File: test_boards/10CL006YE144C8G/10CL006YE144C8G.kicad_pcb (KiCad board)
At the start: 2 copper layers, 90 parts, among them IC1 10CL006YE144C8G, J1 CL_JTAG, U1 W25Q128JVS, Y1 SG-7050CAN

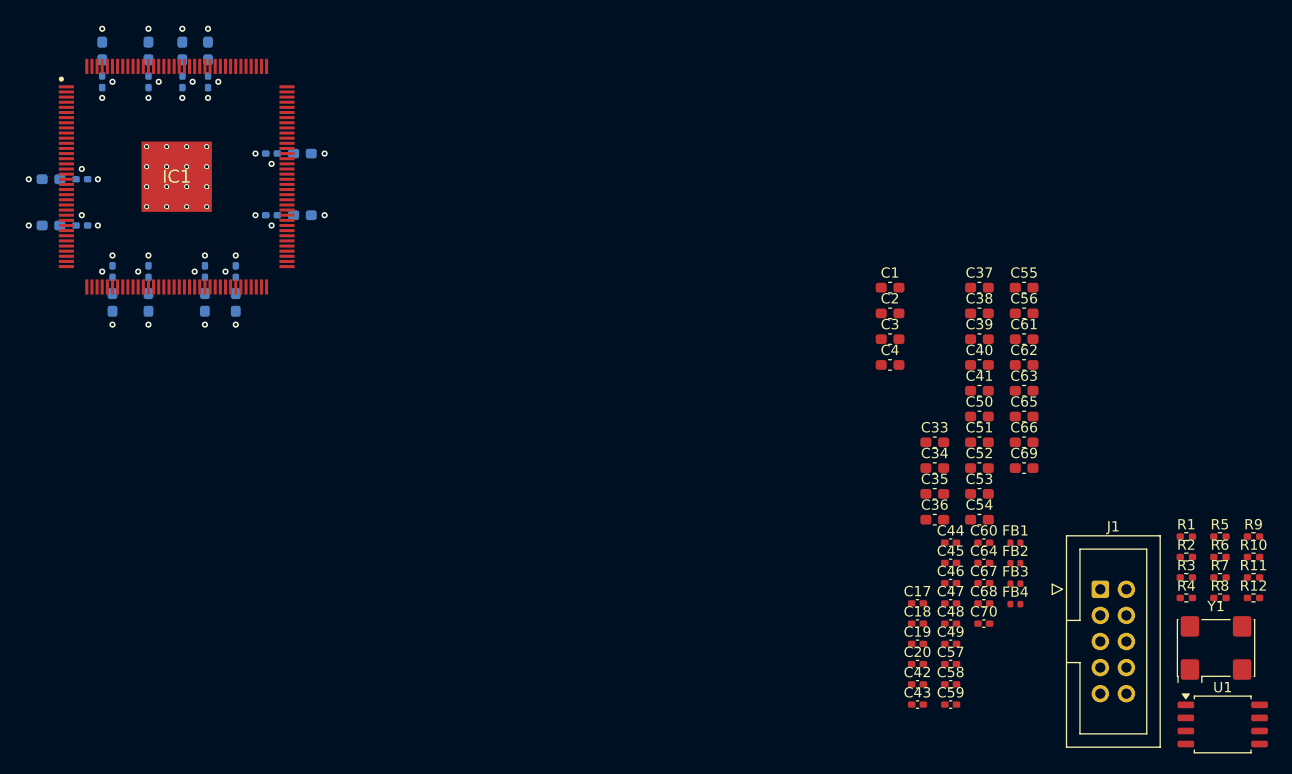
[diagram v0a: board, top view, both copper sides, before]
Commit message: Полный рефакторинг. components может быть несколько. Используются поля KiCad для компонент
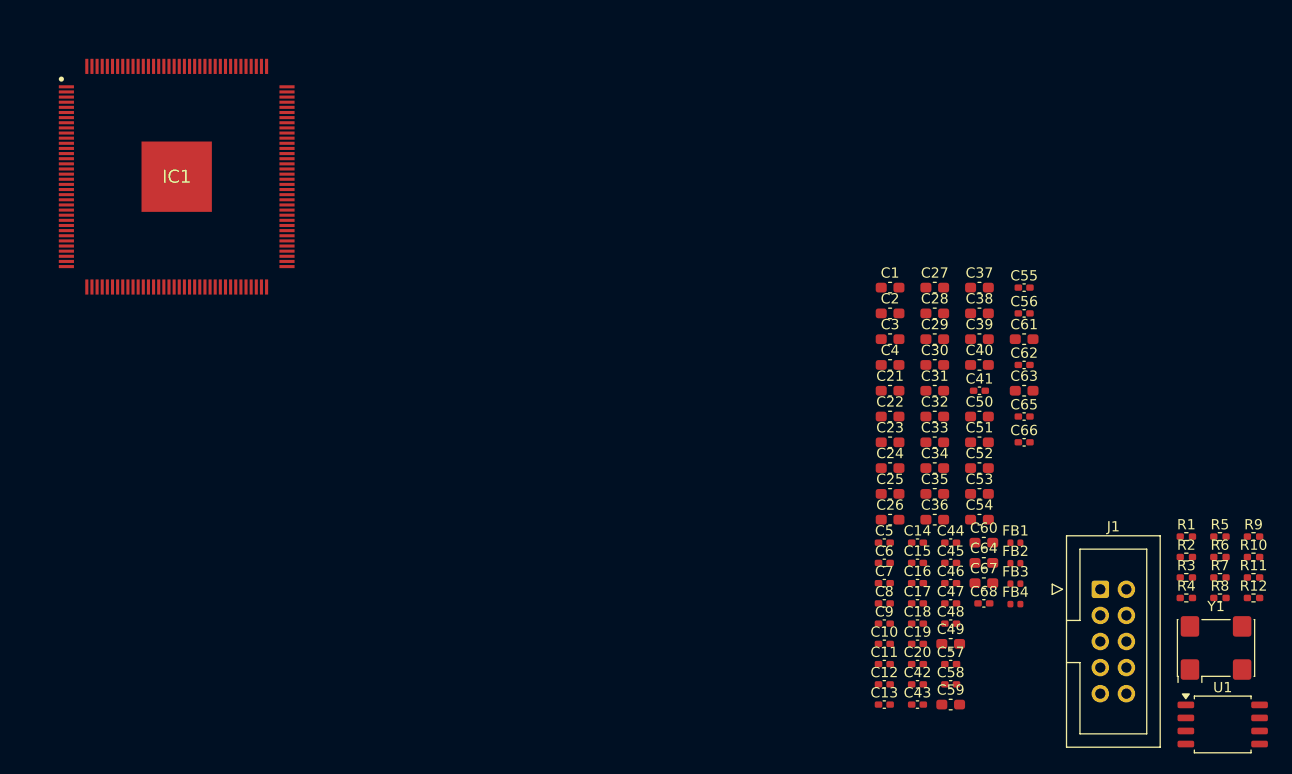
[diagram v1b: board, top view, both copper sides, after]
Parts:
- removed C69: 1uF, Capacitor_SMD:C_0603_1608Metric_Pad1.08x0.95mm_HandSolder
- removed C70: 100 nF, Capacitor_SMD:C_0402_1005Metric_Pad0.74x0.62mm_HandSolder
- C10, C11, C12, C13, C14, C15, C16, C21, C22, C23, C24, C25, C26, C27, C28, C29, C30, C31, C32, C5, C6, C7, C8, C9: moved to F.Cu
- C41, C55, C56, C62: value 4.7 uF -> 100 nF; footprint Capacitor_SMD:C_0603_1608Metric_Pad1.08x0.95mm_HandSolder -> Capacitor_SMD:C_0402_1005Metric_Pad0.74x0.62mm_HandSolder
- C49, C64, C67: value 100 nF -> 1uF; footprint Capacitor_SMD:C_0402_1005Metric_Pad0.74x0.62mm_HandSolder -> Capacitor_SMD:C_0603_1608Metric_Pad1.08x0.95mm_HandSolder
- C50: value 100 nF -> 1uF
- C53, C54: value 1uF -> 4.7 uF
- C59, C60: value 100 nF -> 4.7 uF; footprint Capacitor_SMD:C_0402_1005Metric_Pad0.74x0.62mm_HandSolder -> Capacitor_SMD:C_0603_1608Metric_Pad1.08x0.95mm_HandSolder
- C61: value 4.7 uF -> 1uF
- C65, C66: value 1uF -> 100 nF; footprint Capacitor_SMD:C_0603_1608Metric_Pad1.08x0.95mm_HandSolder -> Capacitor_SMD:C_0402_1005Metric_Pad0.74x0.62mm_HandSolder
- moved C16 93.2 mm to (149.7, 121.2), turned to 0 degrees
- moved C13 89.5 mm to (146.4, 133.0), turned to 0 degrees
- moved C32 88.5 mm to (151.4, 105.0), turned to 0 degrees
- moved C15 88.3 mm to (149.7, 119.2), turned to 0 degrees
- moved C5 85.8 mm to (146.4, 117.2)
- moved C6 84.7 mm to (146.4, 119.2)
- moved C14 84.5 mm to (149.7, 117.2), turned to 0 degrees
- moved C21 84.2 mm to (147.0, 102.4), turned to 0 degrees
- moved C22 83.8 mm to (147.0, 105.0), turned to 0 degrees
- moved C31 83.4 mm to (151.4, 102.4), turned to 0 degrees
- moved C7 81.0 mm to (146.4, 121.2), turned to 0 degrees
- moved C30 79.4 mm to (151.4, 99.9), turned to 0 degrees
- moved C12 78.9 mm to (146.4, 131.0), turned to 0 degrees
- moved C8 78.6 mm to (146.4, 123.1), turned to 0 degrees
- moved C23 76.9 mm to (147.0, 107.5), turned to 0 degrees
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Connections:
- C50 pad 1: +1V2_VCCINT -> +1V2_VCCD_PLL
- C51 pad 1: +1V2_VCCINT -> +2V5_VCCA
- C52 pad 1: +1V2_VCCD_PLL -> +3V3_VCCIO
- C53 pad 1: +2V5_VCCA -> +1V2_VCCD_PLL
- C54 pad 1: +3V3_VCCIO -> +1V2_VCCD_PLL
- C57 pad 1: +1V2_VCCD_PLL -> +2V5_VCCA
- C58 pad 1: +1V2_VCCD_PLL -> +2V5_VCCA
- C61 pad 1: +2V5_VCCA -> +3V3
- C62 pad 1: +2V5_VCCA -> +3V3
- C64 pad 1: +3V3 -> +3V3_OSCILL
- C66 pad 1: +3V3_OSCILL -> GND
- C66 pad 2: GND -> +3V3_OSCILL
- C67 pad 1: +3V3 -> +3V3_FLASH
- C68 pad 2: +3V3_OSCILL -> +3V3_FLASH
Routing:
- net GND: vias 40 -> 0
- net +3V3_VCCIO: vias 12 -> 0

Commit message: Проект переименован в KiCadSpoke
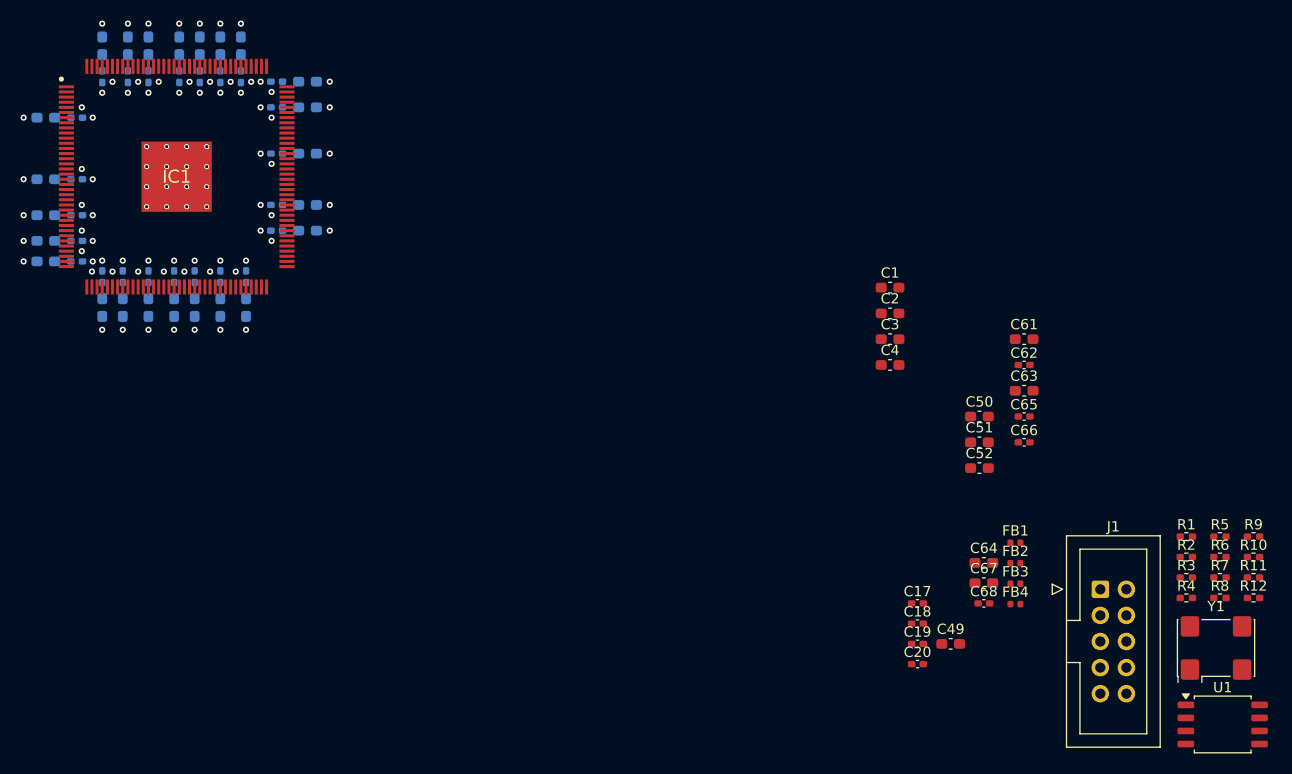
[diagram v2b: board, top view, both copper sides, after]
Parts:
- C10, C11, C12, C13, C14, C15, C16, C21, C22, C23, C24, C25, C26, C27, C28, C29, C30, C31, C32, C5, C57, C58, C59, C6, C60, C7, C8, C9: moved to B.Cu
- C33, C34, C35, C36, C37, C38, C39, C40, C53, C54: value 4.7 uF -> 100 nF; footprint Capacitor_SMD:C_0603_1608Metric_Pad1.08x0.95mm_HandSolder -> Capacitor_SMD:C_0402_1005Metric_Pad0.74x0.62mm_HandSolder; moved to B.Cu
- C41, C42, C43, C44, C45, C46, C47, C48, C55, C56: value 100 nF -> 4.7 uF; footprint Capacitor_SMD:C_0402_1005Metric_Pad0.74x0.62mm_HandSolder -> Capacitor_SMD:C_0603_1608Metric_Pad1.08x0.95mm_HandSolder; moved to B.Cu
- moved C59 98.1 mm to (64.8, 89.9), turned to 180 degrees
- moved C48 97.9 mm to (72.8, 68.9), turned to 90 degrees
- moved C42 95.2 mm to (64.8, 87.9), turned to 180 degrees
- moved C41 94.7 mm to (64.8, 75.9), turned to 180 degrees
- moved C57 93.7 mm to (67.8, 89.9)
- moved C16 93.4 mm to (70.3, 71.9), turned to -90 degrees
- moved C13 90.4 mm to (79.8, 71.9), turned to -90 degrees
- moved C55 89.8 mm to (70.3, 94.3), turned to -90 degrees
- moved C47 89.4 mm to (81.8, 68.9), turned to 90 degrees
- moved C33 89.3 mm to (67.8, 75.9)
- moved C32 88.7 mm to (70.3, 68.9), turned to 90 degrees
- moved C15 88.6 mm to (74.8, 71.9), turned to -90 degrees
- moved C58 88.0 mm to (87.3, 72.4), turned to 180 degrees
- moved C53 88.0 mm to (70.3, 91.3), turned to 90 degrees
- moved C40 87.5 mm to (72.8, 71.9), turned to -90 degrees
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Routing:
- net GND: vias 0 -> 64
- net +3V3_VCCIO: vias 0 -> 12
- net +2V5_VCCA: vias 0 -> 2
- net +1V2_VCCINT: vias 0 -> 8
- net +1V2_VCCD_PLL: vias 0 -> 2
